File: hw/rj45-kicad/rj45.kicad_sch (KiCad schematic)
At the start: 50 parts

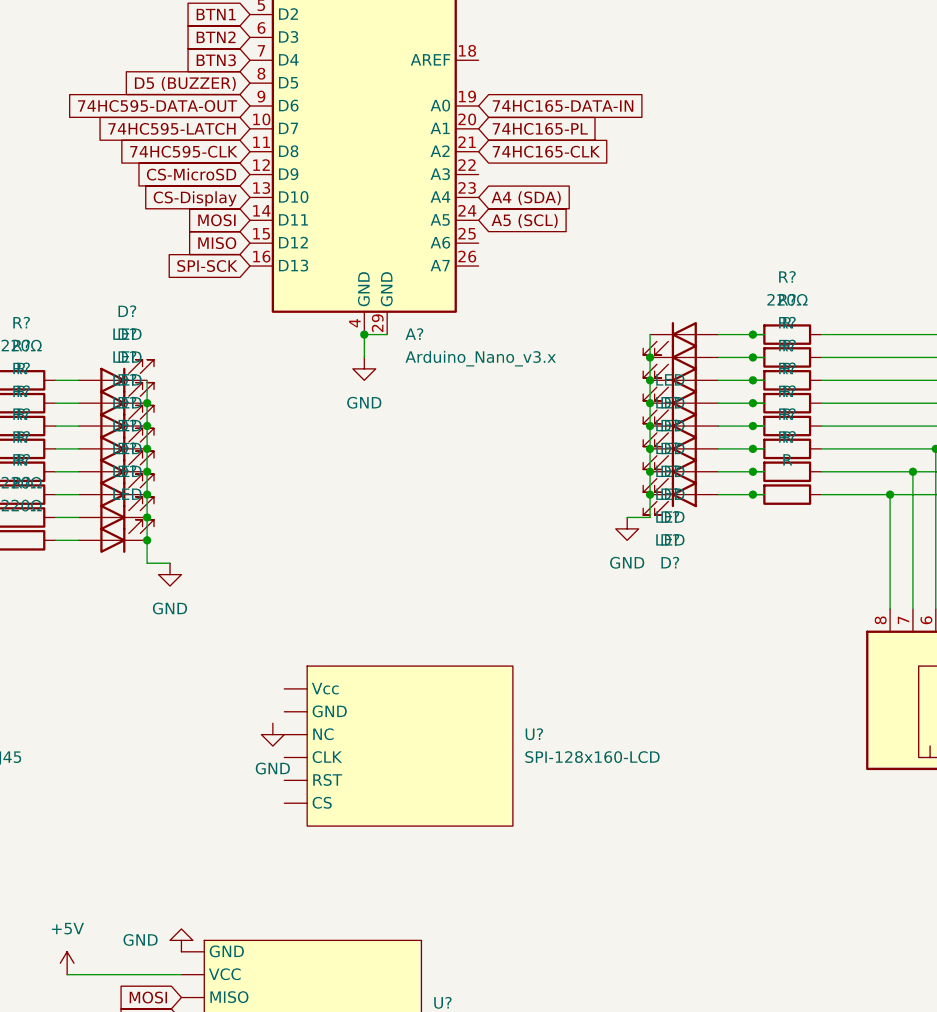
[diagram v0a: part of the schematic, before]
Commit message: Schematics inlcude SPI display
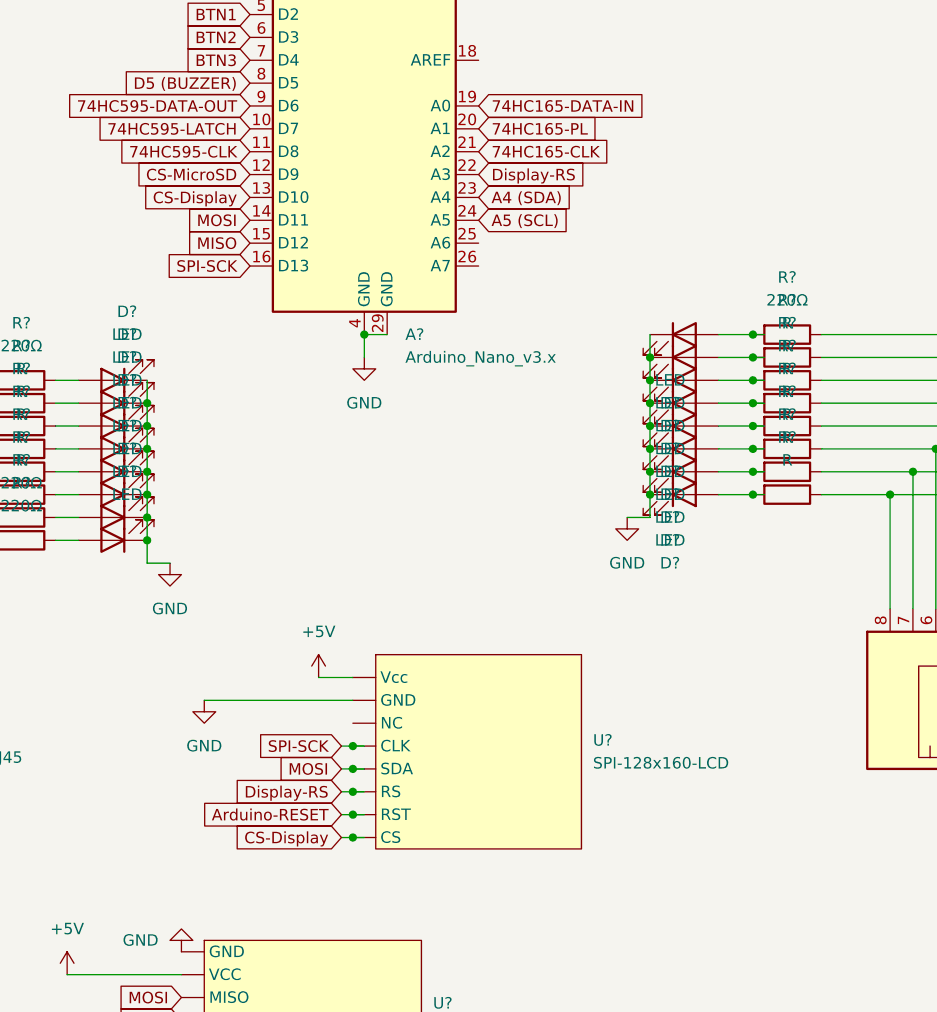
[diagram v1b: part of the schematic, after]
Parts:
- removed U?: SPI-128x160-LCD, symbol custom-parts:SPI-128x160-LCD
- added U?: SPI-128x160-LCD, symbol custom-parts:SPI-128x160-LCD
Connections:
- net +5V: now also U?. (Vcc)
- net CS-Display: now also U?. (Vcc)
- net GND: now also U?. (Vcc)
- net MOSI: now also U?. (Vcc)
- net SPI-SCK: now also U?. (Vcc)
- net Display-RS: now reaches A?.22 (A3)
- net Display-RS: now also U?. (Vcc)
- new net Arduino-RESET: U?. (Vcc)

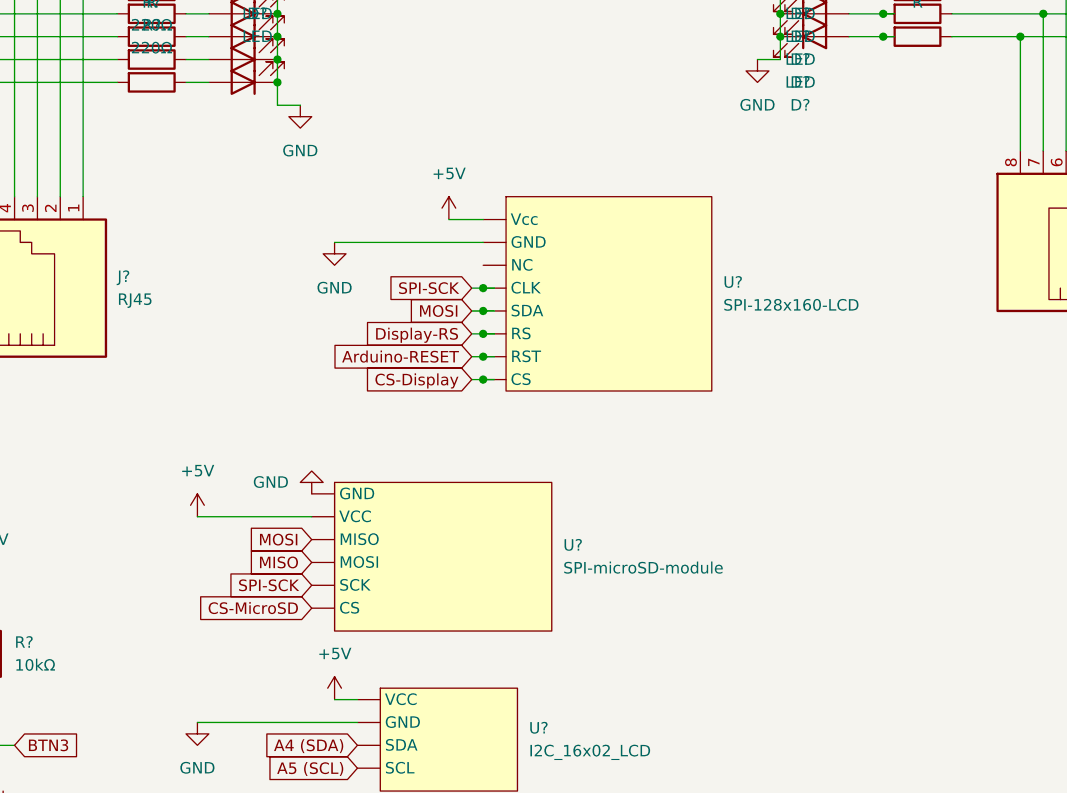
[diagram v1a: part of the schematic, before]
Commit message: Am renuntat la cardul SD
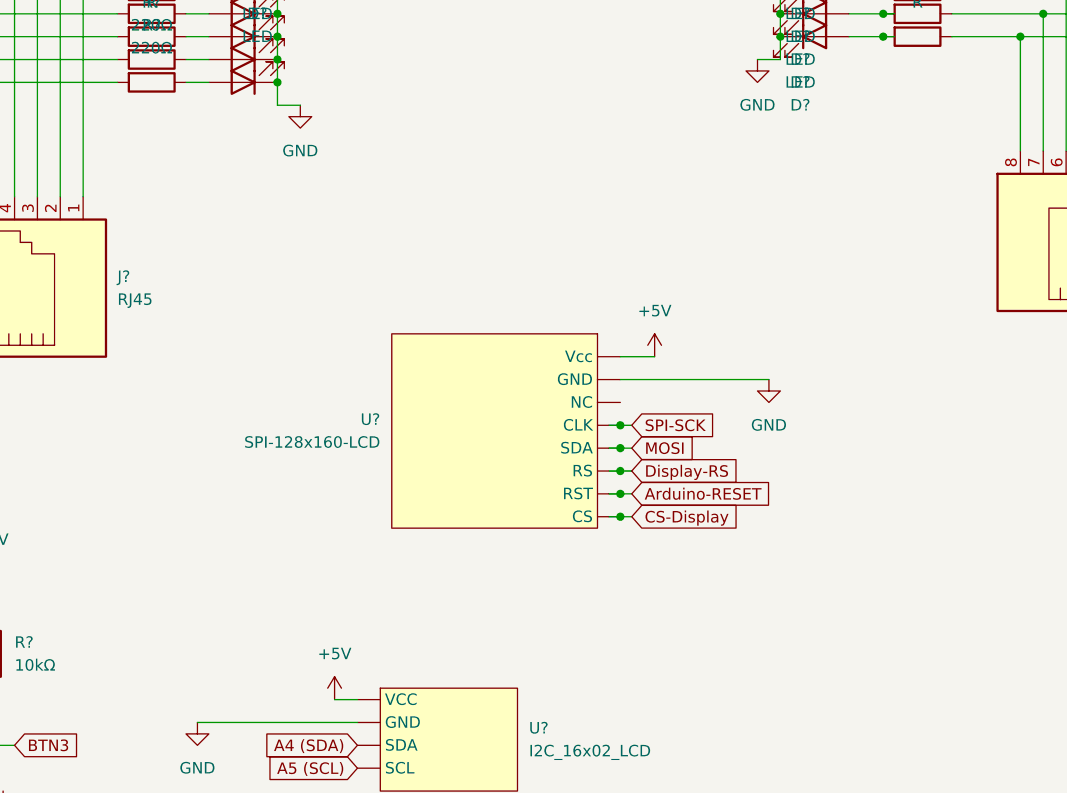
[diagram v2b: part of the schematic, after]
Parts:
- removed U?: SPI-microSD-module, symbol custom-parts:SPI-microSD-module
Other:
- moved on the sheet: U?

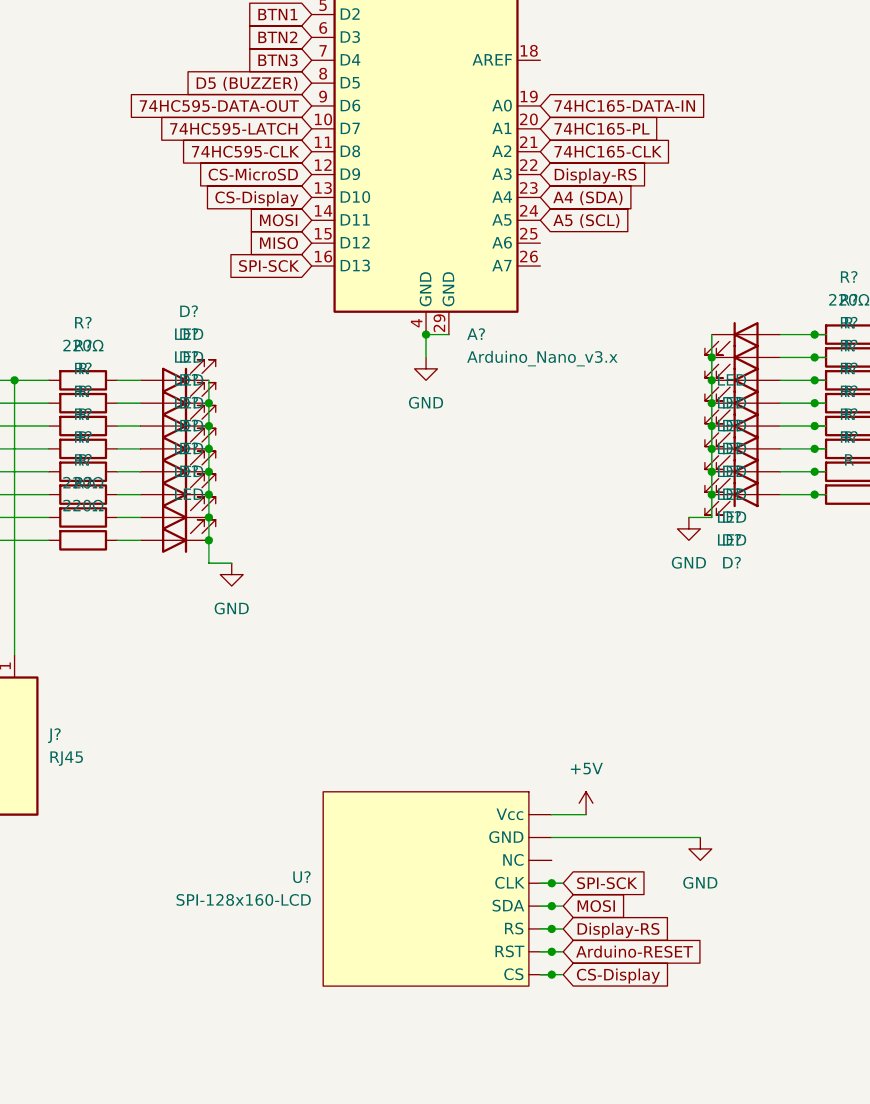
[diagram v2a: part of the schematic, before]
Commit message: README: detailed pin configs
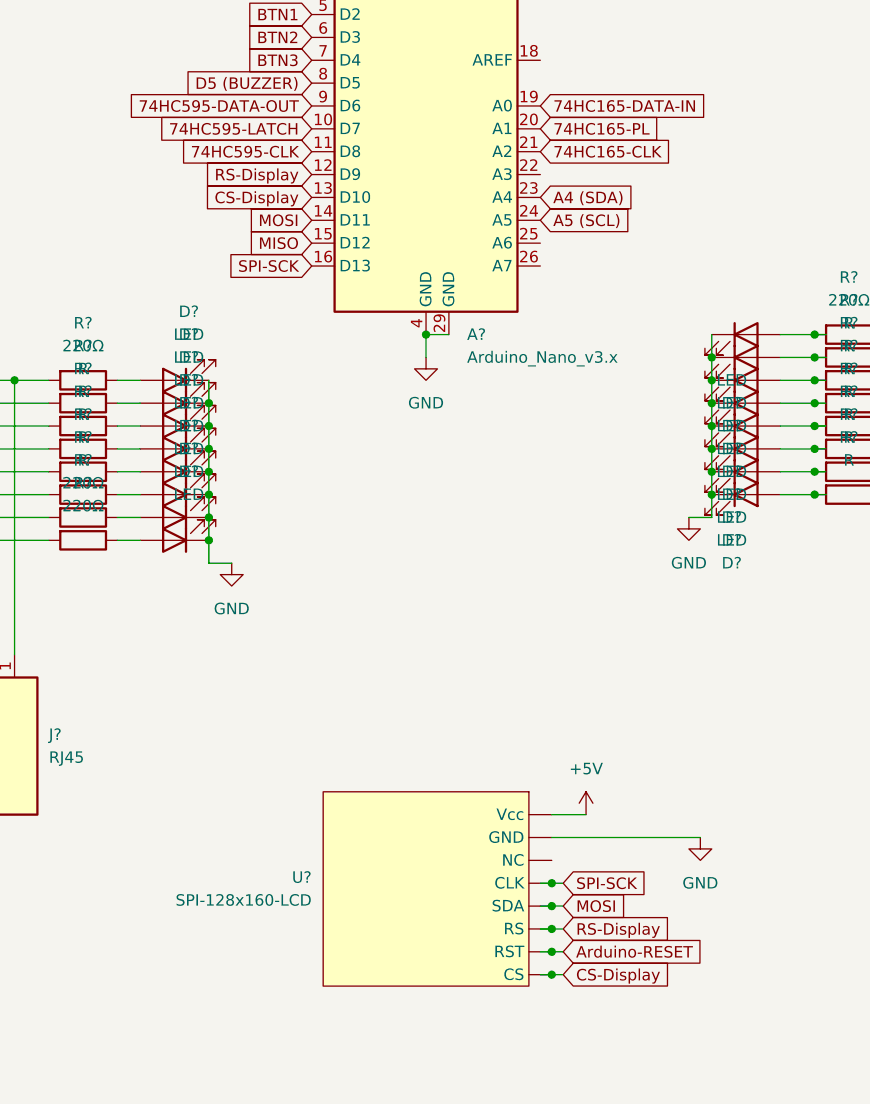
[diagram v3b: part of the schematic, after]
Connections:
- net CS-MicroSD renamed RS-Display
- net RS-Display: now also U?. (Vcc)
- net Display-RS: no longer names the net of A?.22 (A3)
- net Display-RS: no longer U?. (Vcc)
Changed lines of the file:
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@@
     (stroke (width 0) (type default) (color 0 0 0 0))
-  )
-  (global_label "CS-MicroSD" (shape input) (at 129.54 53.34 180) (fields_autoplaced)
-    (effects (font (size 1.27 1.27)) (justify right))
-    (property "Intersheet References" "${INTERSHEET_REFS}" (id 0) (at 115.5155 53.2606 0)
-      (effects (font (size 1.27 1.27)) (justify right) hide)
-    )
   )
   (global_label "74HC595-LATCH" (shape input) (at 35.56 81.28 180) (fields_autoplaced)
@@
     )
   )
-  (global_label "Display-RS" (shape input) (at 154.94 53.34 0) (fields_autoplaced)
-    (effects (font (size 1.27 1.27)) (justify left))
-    (property "Intersheet References" "${INTERSHEET_REFS}" (id 0) (at 168.2388 53.2606 0)
-      (effects (font (size 1.27 1.27)) (justify left) hide)
+  (global_label "RS-Display" (shape input) (at 129.54 53.34 180) (fields_autoplaced)
+    (effects (font (size 1.27 1.27)) (justify right))
+    (property "Intersheet References" "${INTERSHEET_REFS}" (id 0) (at 116.2412 53.2606 0)
+      (effects (font (size 1.27 1.27)) (justify right) hide)
     )
   )
@@
     )
   )
-  (global_label "Display-RS" (shape input) (at 157.48 137.16 0) (fields_autoplaced)
+  (global_label "RS-Display" (shape input) (at 157.48 137.16 0) (fields_autoplaced)
     (effects (font (size 1.27 1.27)) (justify left))
     (property "Intersheet References" "${INTERSHEET_REFS}" (id 0) (at 170.7788 137.0806 0)
